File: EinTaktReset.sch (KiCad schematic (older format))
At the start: 57 parts, among them IC1 74LS624, J1 3PinTerminalBlocktg, J2 3PinTerminalBlocktg, P1 CONN_02X10, P2 CONN_01X01, P3 CONN_01X01, P4 CONN_02X10, P8 CONN_01X01, P9 CONN_01X01, SW1 SPST, SW10 SPST, SW11 SPST, SW12 SPST, SW13 SPST, SW2 SWITCH_INV, SW3 SPST, SW4 SPST, SW5 SPST, SW6 SWITCH_INV, SW7 SPST, SW8 SPST, SW9 SPST, U1 74LS132, U2 74540En, U3 74HCT541_PWR, U4 74LS32, U5 74LS00, U6 74LS132

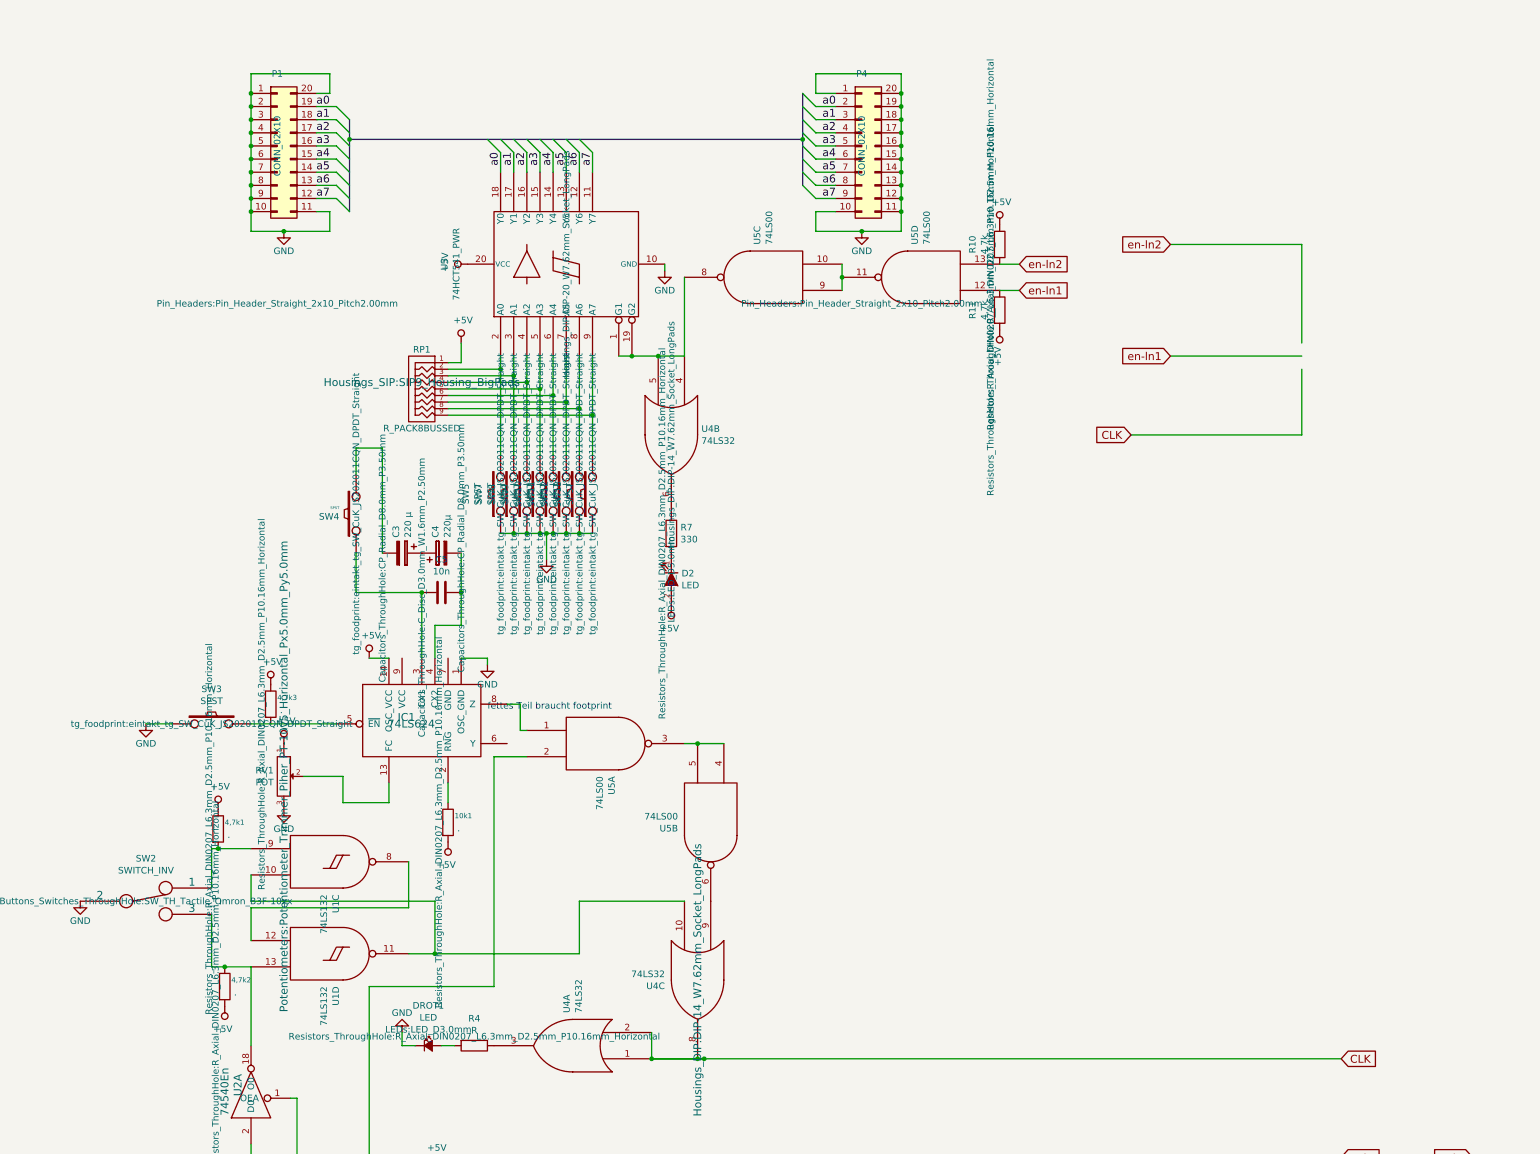
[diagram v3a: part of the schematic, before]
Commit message: Pin Header reorganized localy and adapted
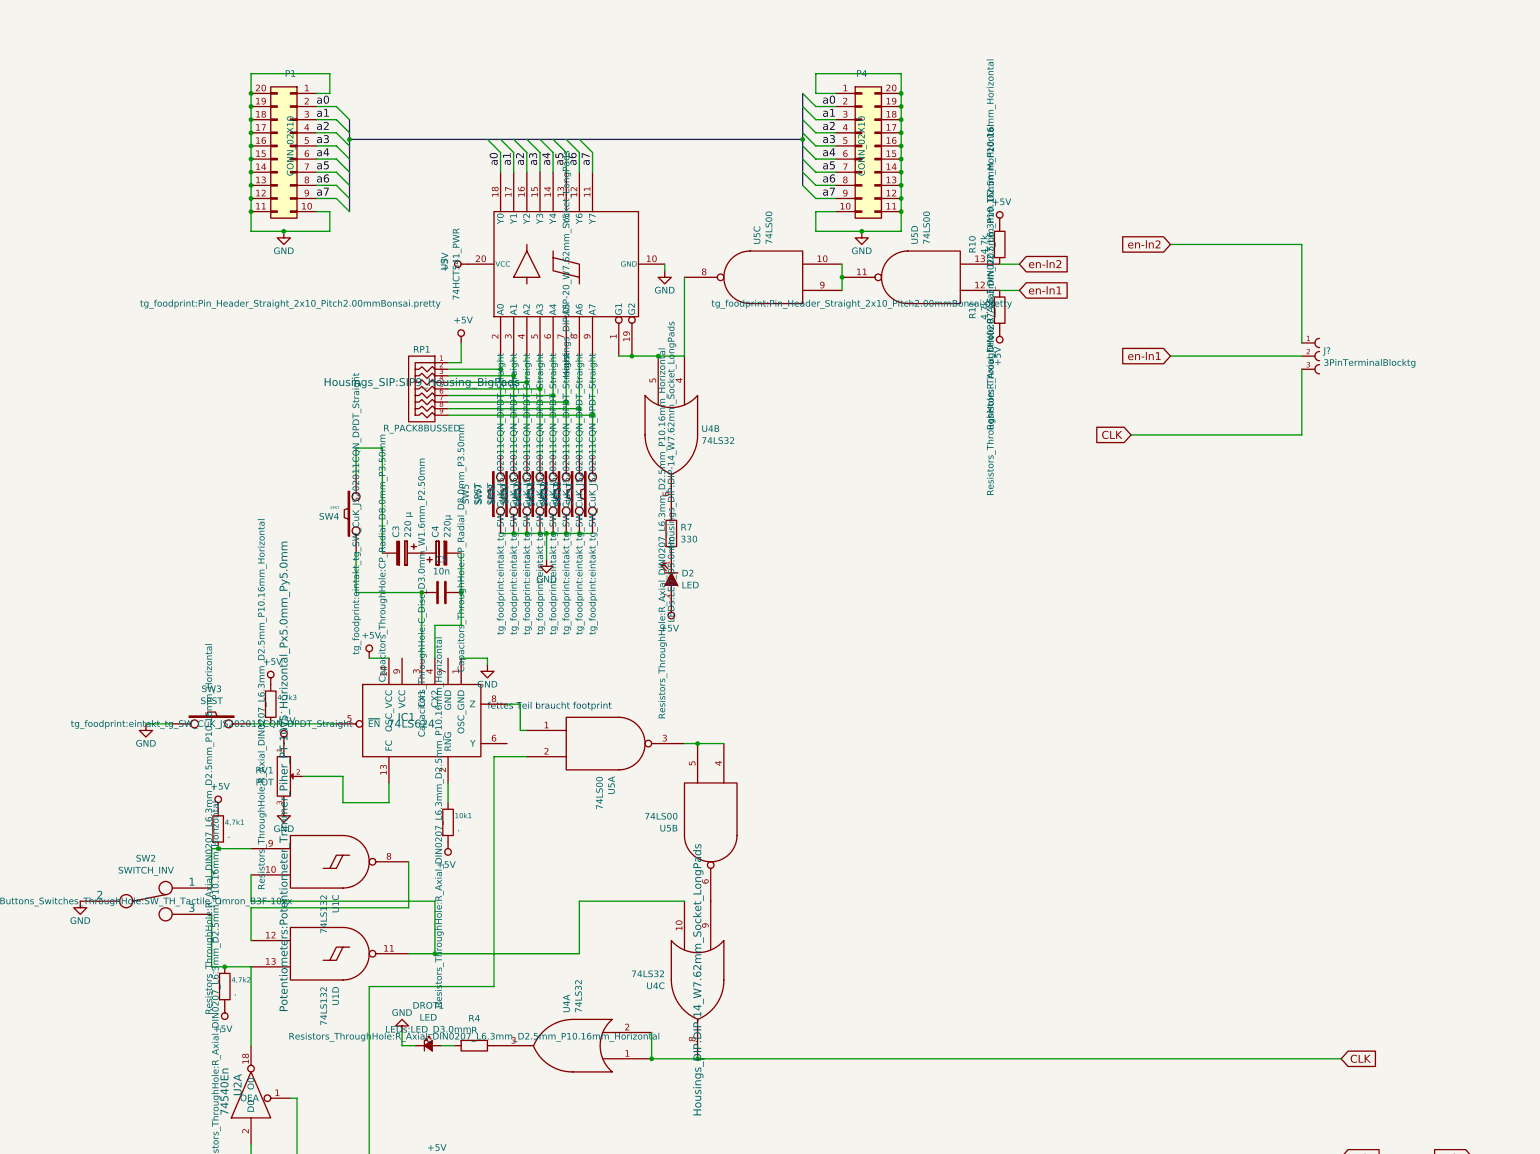
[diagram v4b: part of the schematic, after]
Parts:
- added J?: 3PinTerminalBlocktg, 3PinTerminalBlocktg, symbol 3PinTerminalBlocktg:3PinTerminalBlocktg
- P1, P4: footprint Pin_Headers:Pin_Header_Straight_2x10_Pitch2.00mm -> tg_foodprint:Pin_Header_Straight_2x10_Pitch2.00mmBonsai.pretty
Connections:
- net CLK: now also J?.3
- net GND: now also P1.12 (Pin_12), P1.13 (Pin_13), P1.14 (Pin_14), P1.15 (Pin_15), P1.16 (Pin_16), P1.17 (Pin_17), P1.18 (Pin_18), P1.19 (Pin_19); no longer P1.2 (Pin_2), P1.3 (Pin_3), P1.4 (Pin_4), P1.5 (Pin_5), P1.6 (Pin_6), P1.7 (Pin_7), P1.8 (Pin_8), P1.9 (Pin_9)
- net a0: now also P1.2 (Pin_2); no longer P1.19 (Pin_19)
- net a1: now also P1.3 (Pin_3); no longer P1.18 (Pin_18)
- net a2: now also P1.4 (Pin_4); no longer P1.17 (Pin_17)
- net a3: now also P1.5 (Pin_5); no longer P1.16 (Pin_16)
- net a4: now also P1.6 (Pin_6); no longer P1.15 (Pin_15)
- net a5: now also P1.7 (Pin_7); no longer P1.14 (Pin_14)
- net a6: now also P1.8 (Pin_8); no longer P1.13 (Pin_13)
- net a7: now also P1.9 (Pin_9); no longer P1.12 (Pin_12)
- net en-ln1: now also J?.2
- net en-ln2: now also J?.1
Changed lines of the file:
@@
 F 0 "P4" H 7000 2100 50  0000 C CNN
 F 1 "CONN_02X10" V 7000 1550 50  0000 C CNN
-F 2 "Pin_Headers:Pin_Header_Straight_2x10_Pitch2.00mm" H 7000 350 50  0000 C CNN
+F 2 "tg_foodprint:Pin_Header_Straight_2x10_Pitch2.00mmBonsai.pretty" H 7000 350 50  0000 C CNN
 F 3 "" H 7000 350 50  0000 C CNN
 	1    7000 1550
@@
 L conn:Conn_02x10_Counter_Clockwise P1
 U 1 1 5A2833E0
-P 2550 1550
-F 0 "P1" H 2550 2100 50  0000 C CNN
-F 1 "CONN_02X10" V 2550 1550 50  0000 C CNN
-F 2 "Pin_Headers:Pin_Header_Straight_2x10_Pitch2.00mm" H 2550 350 50  0000 C CNN
-F 3 "" H 2550 350 50  0000 C CNN
-	1    2550 1550
-	1    0    0    -1
+P 2650 1550
+F 0 "P1" H 2650 2100 50  0000 C CNN
+F 1 "CONN_02X10" V 2650 1550 50  0000 C CNN
+F 2 "tg_foodprint:Pin_Header_Straight_2x10_Pitch2.00mmBonsai.pretty" H 2650 350 50  0000 C CNN
+F 3 "" H 2650 350 50  0000 C CNN
+	1    2650 1550
+	-1   0    0    -1
 $EndComp
 $Comp
@@
 Wire Wire Line
 	5400 8300 5400 8500
-Wire Wire Line
-	5400 8500 5750 8500
+Connection ~ 5400 8500
+Connection ~ 5750 8500
+Wire Wire Line
+	5750 8500 5800 8500
+Wire Wire Line
+	5750 8500 10650 8500
 Wire Bus Line
 	3100 1350 3100 1500
@@
 Wire Bus Line
 	3100 1500 6550 1500
-Connection ~ 5400 8500
-Connection ~ 5800 8500
-Wire Wire Line
-	5800 8500 10650 8500
-Connection ~ 5750 8500
-Wire Wire Line
-	5750 8500 5800 8500
-Wire Wire Line
-	5750 8500 5800 8500
+$Comp
+L 3PinTerminalBlocktg:3PinTerminalBlocktg J?
+U 1 1 5AC39ABD
+P 10550 3150
+F 0 "J?" H 10515 3190 50  0000 L CNN
+F 1 "3PinTerminalBlocktg" H 10515 3099 50  0000 L CNN
+F 2 "3PinTerminalBlocktg" H 10550 3150 50  0001 L BNN
+F 3 "1.12 USD" H 10550 3150 50  0001 L BNN
+F 4 "Warning" H 10550 3150 50  0001 L BNN "Field4"
+F 5 "Wurth Electronics" H 10550 3150 50  0001 L BNN "Field5"
+F 6 "TERM BLK 5MM HORZ ENTRY MOD 3P" H 10550 3150 50  0001 L BNN "Field6"
+F 7 "None" H 10550 3150 50  0001 L BNN "Field7"
+F 8 "3PinTerminalBlocktg" H 10550 3150 50  0001 L BNN "Field8"
+	1    10550 3150
+	1    0    0    -1
+$EndComp
 $EndSCHEMATC

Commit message: Didoe Footpront
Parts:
- D3: footprint (none) -> LEDs:LED_D1.8mm_W1.8mm_H2.4mm_Horizontal_O1.27mm_Z4.9mm
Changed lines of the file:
@@
 F 0 "D3" H 3850 15585 50  0000 C CNN
 F 1 "D" H 3850 15676 50  0000 C CNN
-F 2 "" H 3850 15800 60  0000 C CNN
+F 2 "LEDs:LED_D1.8mm_W1.8mm_H2.4mm_Horizontal_O1.27mm_Z4.9mm" H 3850 15800 60  0000 C CNN
 F 3 "" H 3850 15800 60  0000 C CNN
 	1    3850 15800
@@
 Wire Wire Line
 	5750 8500 10650 8500
-Wire Bus Line
-	3100 1350 3100 1500
-Wire Bus Line
-	6550 1150 6550 1500
-Wire Bus Line
-	6550 1500 6550 1850
-Wire Bus Line
-	3100 1500 3100 2050
-Wire Bus Line
-	3100 1500 6550 1500
 $Comp
 L 3PinTerminalBlocktg:3PinTerminalBlocktg J?
@@
 	1    0    0    -1
 $EndComp
+Wire Bus Line
+	3100 1350 3100 1500
+Wire Bus Line
+	6550 1150 6550 1500
+Wire Bus Line
+	6550 1500 6550 1850
+Wire Bus Line
+	3100 1500 3100 2050
+Wire Bus Line
+	3100 1500 6550 1500
 $EndSCHEMATC

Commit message: EintaktReset.todo done
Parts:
- removed J?: 3PinTerminalBlocktg, 3PinTerminalBlocktg, symbol 3PinTerminalBlocktg:3PinTerminalBlocktg
- removed P2, P3, P8, P9: CONN_01X01, Connect:1pin, symbol conn:Conn_01x01
- removed R14: R, symbol bonsai:R
- added C? (x4): 100n, symbol bonsai:C
- added J? (x2): 2PinTerminalBlocktg, 2PinTerminalBlocktg, symbol 2PinTerminalBlocktg:2PinTerminalBlocktg
- added J?: 3PinTerminalBlocktg, 3PinTerminalBlocktg, symbol 3PinTerminalBlocktg:3PinTerminalBlocktg
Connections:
- net CLK: now also J2.1
- net GND: now also C?.2, C?.2, C?.2, C?.2, J?.1
- net VCC: now also C?.1, C?.1, C?.1, C?.1, J?.2
- net auto: now also J1.3; no longer J2.1
- net clrAkku: now also J?.2
- net clrMPC: now also J?.1; no longer J1.1
- net clrPC: now also J?.1
- net en-ln1: now also J1.1
- net en-ln2: now also J1.2
- net enAkku: now also J?.2; no longer J1.2
- net enDEC: now also J2.2; no longer J2.3
- net enSTW: now also J2.3; no longer J2.2
- net loadIR: now also J?.3; no longer J1.3
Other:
- moved on the sheet: D3, J1, J2
